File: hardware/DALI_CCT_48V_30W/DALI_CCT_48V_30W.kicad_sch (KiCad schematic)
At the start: 0 parts

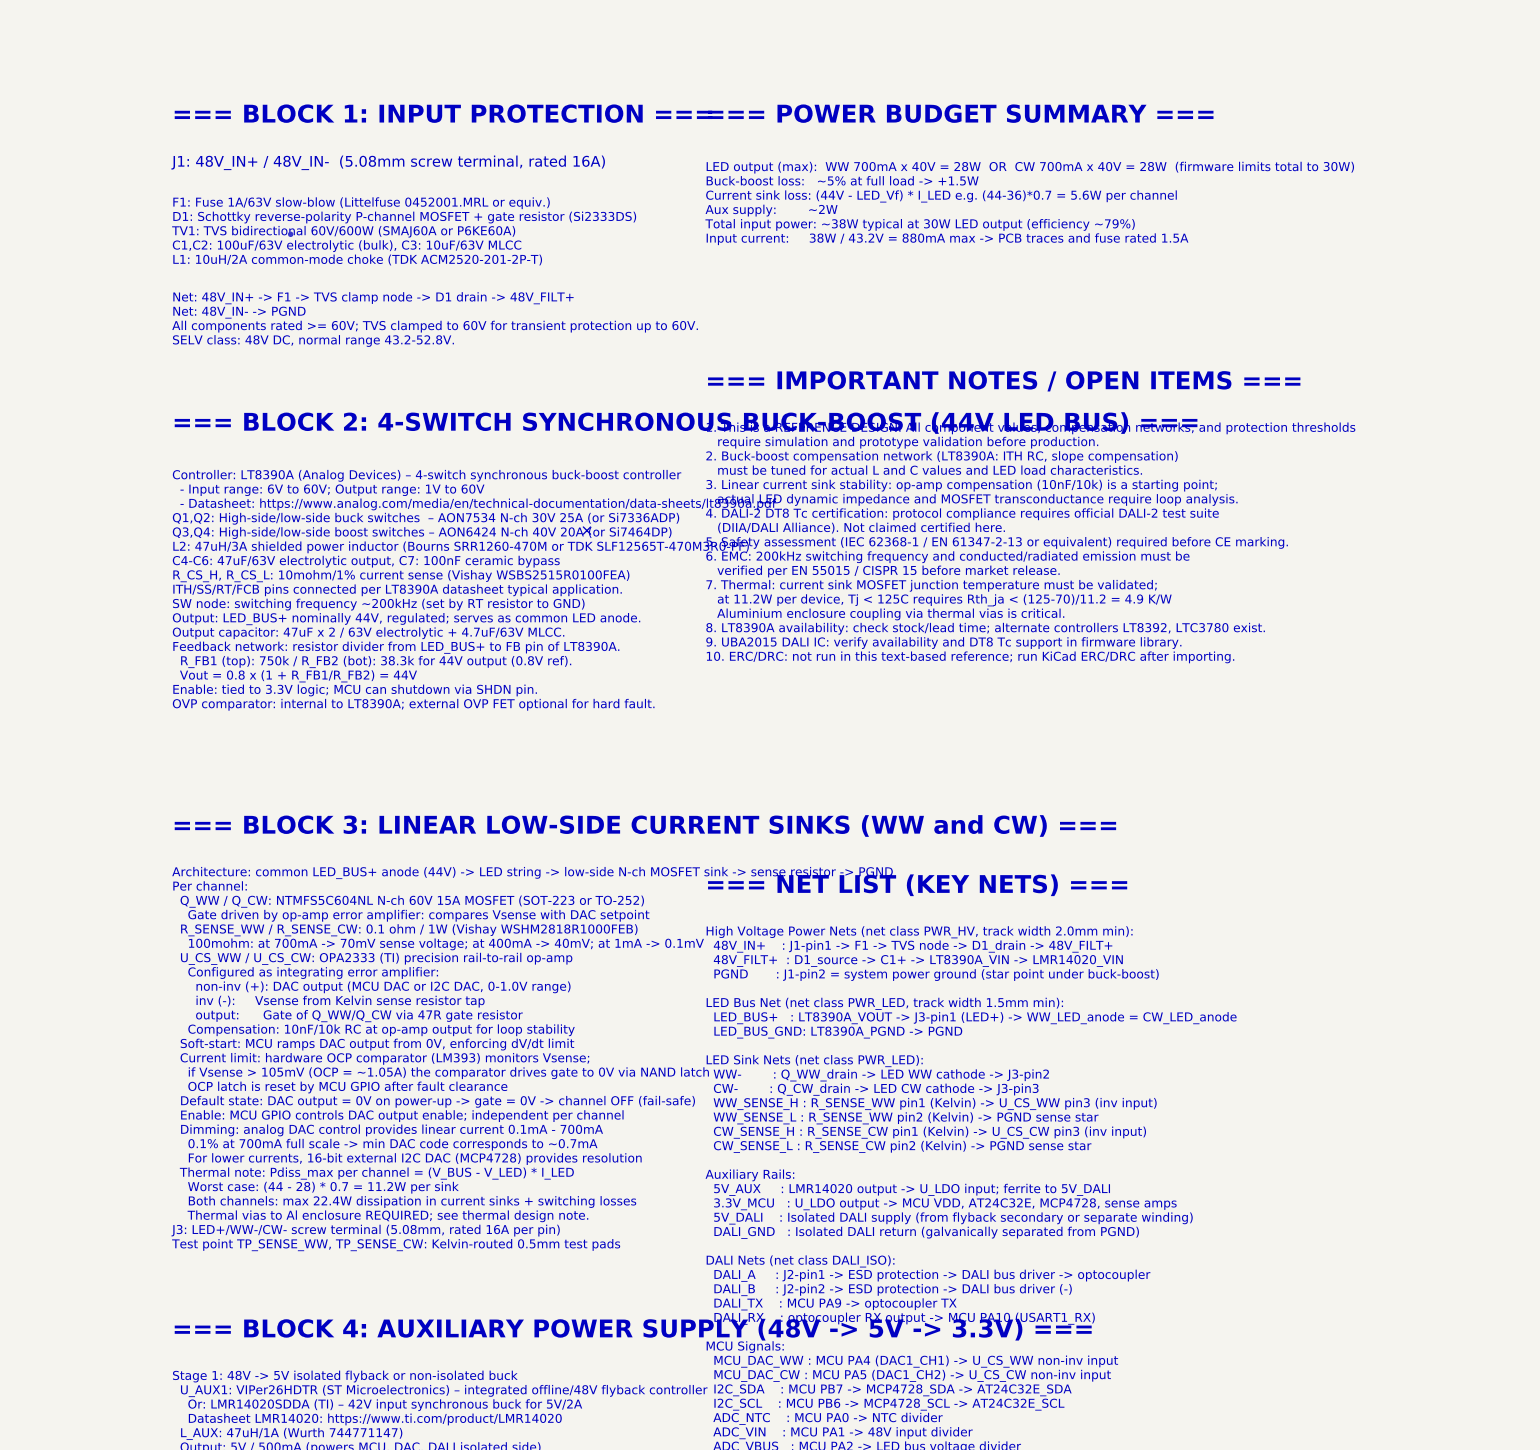
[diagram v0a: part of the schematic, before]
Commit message: Schritt 3: KiCad Schaltplan und PCB-Layout ergänzt (OI-011/OI-012)
Co-authored-by: manuelh83 <208121220+manuelh83@users.noreply.github.com>
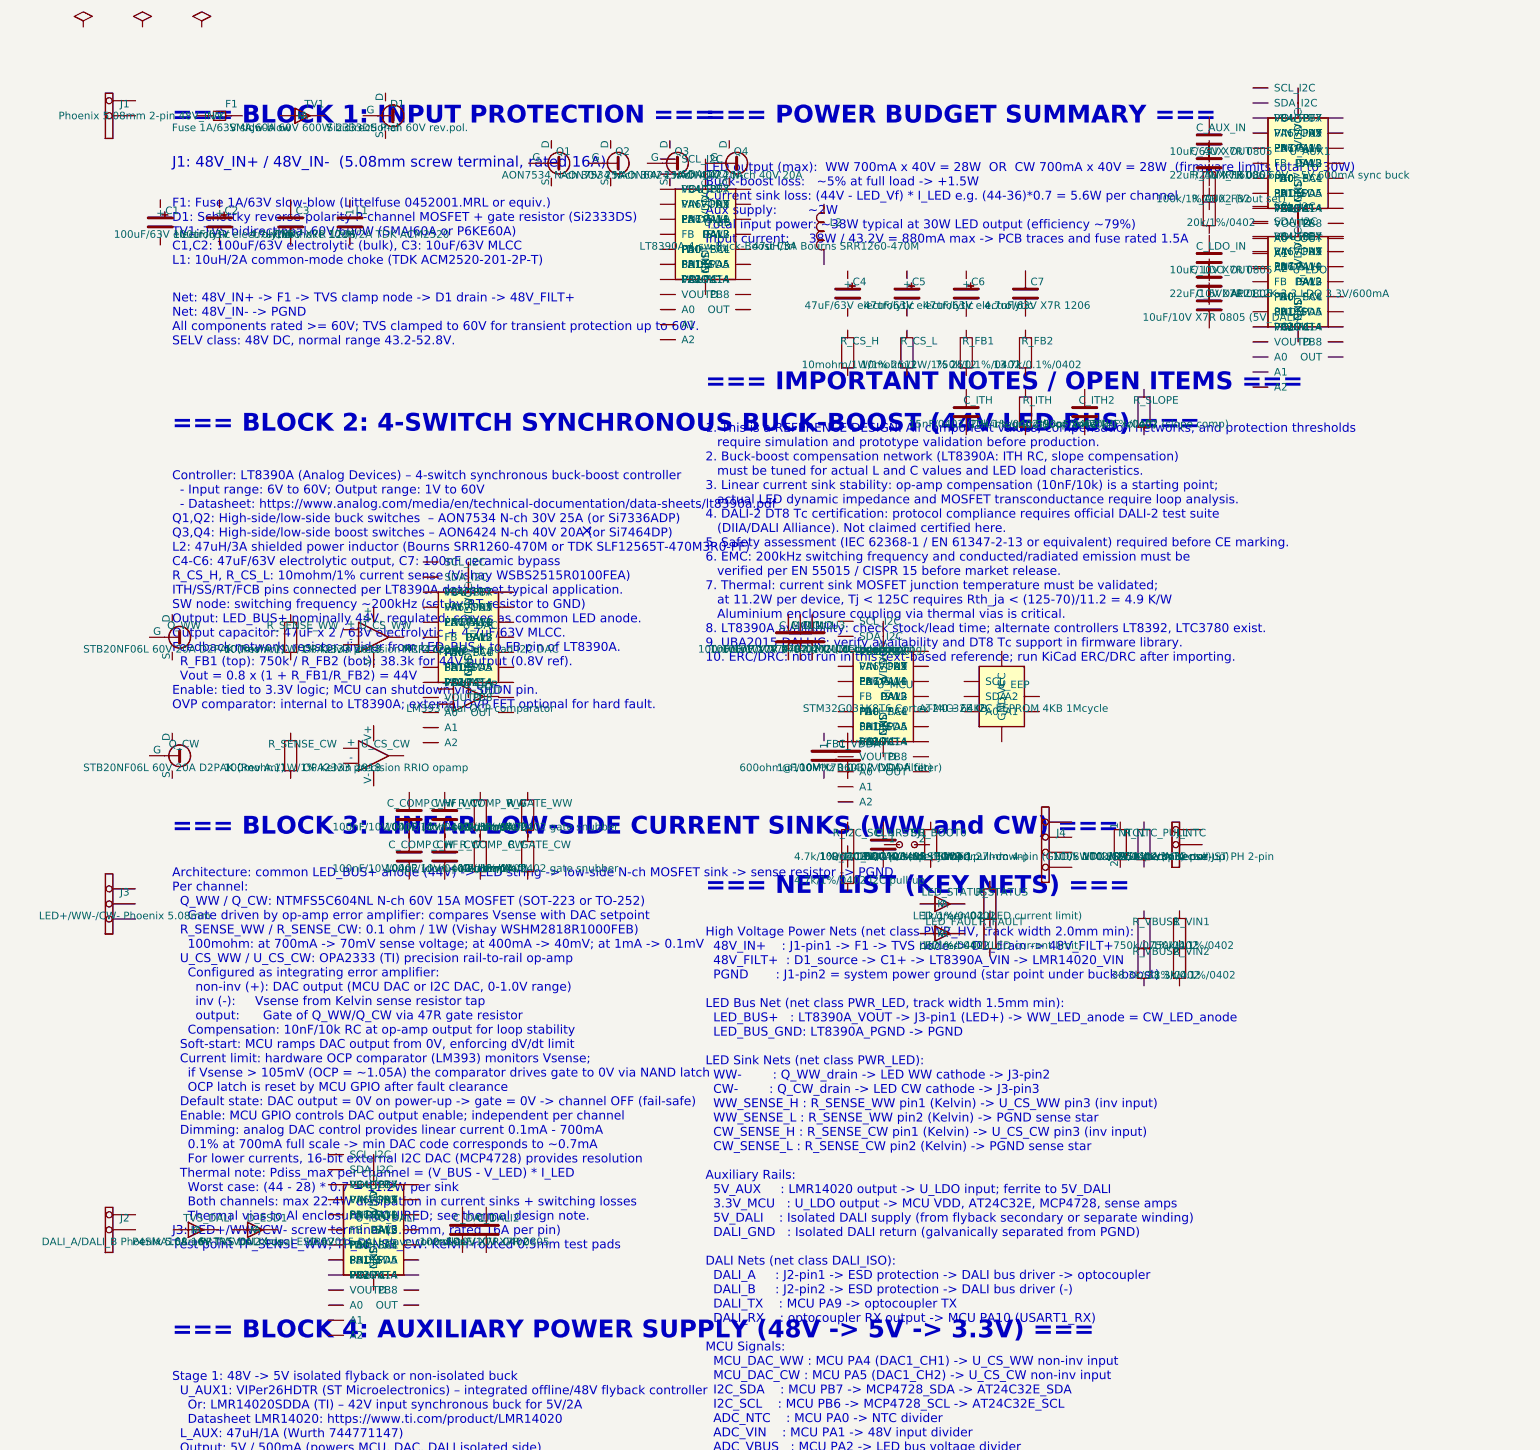
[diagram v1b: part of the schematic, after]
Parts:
- added C1, C2: 100uF/63V electrolytic, Capacitor_THT:CP_Radial_D5.0mm_P2.50mm, symbol Device:CP
- added C3, C7: 4.7uF/63V X7R 1206, Capacitor_SMD:C_1206_3216Metric, symbol Device:C
- added C4, C5, C6: 47uF/63V electrolytic, Capacitor_THT:CP_Radial_D5.0mm_P2.50mm, symbol Device:CP
- added C_5VDALI: 10uF/10V X7R 0805 (5V_DALI), Capacitor_SMD:C_0805_2012Metric, symbol Device:C
- added C_AUX_IN: 10uF/63V X7R 0805, Capacitor_SMD:C_0805_2012Metric, symbol Device:C
- added C_AUX_OUT: 22uF/25V X7R 0805, Capacitor_SMD:C_0805_2012Metric, symbol Device:C
- added C_COMP_CW, C_COMP_WW: 100nF/10V/0402 (dom.pole comp), Capacitor_SMD:C_0402_1005Metric, symbol Device:C
- added C_DALI1: 100nF/10V X7R 0402, Capacitor_SMD:C_0402_1005Metric, symbol Device:C
- added C_DALI2, C_LDO_IN: 10uF/10V X7R 0805, Capacitor_SMD:C_0805_2012Metric, symbol Device:C
- added C_HF_CW, C_HF_WW: 100pF/10V/0402 (HF rolloff), Capacitor_SMD:C_0402_1005Metric, symbol Device:C
- added C_ITH: 15nF/0402 (ITH integrator), Capacitor_SMD:C_0402_1005Metric, symbol Device:C
- added C_ITH2: 390pF/0402 (HF rolloff), Capacitor_SMD:C_0402_1005Metric, symbol Device:C
- added C_LDO_OUT: 22uF/10V X7R 0805, Capacitor_SMD:C_0805_2012Metric, symbol Device:C
- added C_MCU1, C_MCU2, C_MCU3: 100nF/10V X7R 0402 (MCU decoupling), Capacitor_SMD:C_0402_1005Metric, symbol Device:C
- added C_NRST: 100nF/10V/0402 (NRST filter), Capacitor_SMD:C_0402_1005Metric, symbol Device:C
- added C_VDDA: 1uF/10V X7R 0402 (VDDA filter), Capacitor_SMD:C_0402_1005Metric, symbol Device:C
- added D1: Si2333DS P-ch 60V rev.pol., Package_TO_SOT_SMD:SOT-23, symbol Device:MOSFET_P
- added D_ESD1: PRTR5V0U2X dual ESD 5V, Package_TO_SOT_SMD:SOT-363_Handsoldering, symbol Device:D_Schottky
- added F1: Fuse 1A/63V slow-blow, Fuse:Fuse_0402_1005Metric, symbol Device:Fuse
- added FB1: 600ohm@100MHz 0603 (VDDA filter), Inductor_SMD:L_0603_1608Metric, symbol Device:Ferrite_Bead
- added J1: Phoenix 5.08mm 2-pin 48V_IN, Connector_PinHeader_5.08mm:PinHeader_1x02_P5.08mm_Vertical, symbol Connector_Generic:Conn_01x02
- added J2: DALI_A/DALI_B Phoenix 5.08mm, Connector_PinHeader_5.08mm:PinHeader_1x02_P5.08mm_Vertical, symbol Connector_Generic:Conn_01x02
- added J3: LED+/WW-/CW- Phoenix 5.08mm, Connector_PinHeader_5.08mm:PinHeader_1x03_P5.08mm_Vertical, symbol Connector_Generic:Conn_01x03
- added J4: SWD 1.27mm 4-pin (GND/SWDIO/SWDCLK/3V3), Connector_PinHeader_1.27mm:PinHeader_1x04_P1.27mm_SMD, symbol Connector_Generic:Conn_01x04
- added J_NTC: NTC ext. connector JST PH 2-pin, Connector_JST:JST_PH_B2B-PH-K_1x02_P2.00mm_Vertical, symbol Connector_Generic:Conn_01x02
- added L1: CM choke 10uH/2A TDK ACM2520, Inductor_SMD:L_2520_6332Metric, symbol Device:Ferrite_Bead
- added L2: 47uH/3A Bourns SRR1260-470M, Inductor_SMD:L_Bourns_SRR1260, symbol Device:L
- added LED_FAULT: LED red 0402, LED_SMD:LED_0402_1005Metric, symbol Device:LED
- added LED_STATUS: LED green 0402, LED_SMD:LED_0402_1005Metric, symbol Device:LED
- added NTC1: 100k NTC B3950 (temp sense), Resistor_SMD:R_0402_1005Metric, symbol Device:R_Thermistor_NTC
- added Q1, Q2: AON7534 N-ch 30V 25A, Package_TO_SOT_SMD:DFN-8-1EP_3x3mm_P0.65mm, symbol Device:MOSFET_N
- added Q3, Q4: AON6424 N-ch 40V 20A, Package_TO_SOT_SMD:DFN-8-1EP_3x3mm_P0.65mm, symbol Device:MOSFET_N
- added Q_CW, Q_WW: STB20NF06L 60V 20A D2PAK (Rev A.1), Package_TO_SOT_SMD:TO-263-3_TabDown, symbol Device:MOSFET_N
- added R_AUX_FB1: 100k/1%/0402 (Vout set), Resistor_SMD:R_0402_1005Metric, symbol Device:R
- added R_AUX_FB2: 20k/1%/0402, Resistor_SMD:R_0402_1005Metric, symbol Device:R
- added R_BOOT0: 10k/1%/0402 (BOOT0 pull-down), Resistor_SMD:R_0402_1005Metric, symbol Device:R
- added R_COMP_CW, R_COMP_WW: 10k/1%/0402, Resistor_SMD:R_0402_1005Metric, symbol Device:R
- added R_CS_H, R_CS_L: 10mohm/1W/1% 2512, Resistor_SMD:R_2512_6332Metric, symbol Device:R
- added R_FAULT, R_STATUS: 1k/1%/0402 (LED current limit), Resistor_SMD:R_0402_1005Metric, symbol Device:R
- added R_FB1, R_VBUS1, R_VIN1: 750k/0.1%/0402, Resistor_SMD:R_0402_1005Metric, symbol Device:R
- added R_FB2: 13.7k/0.1%/0402, Resistor_SMD:R_0402_1005Metric, symbol Device:R
- added R_GATE_CW, R_GATE_WW: 47ohm/1%/0402 gate snubber, Resistor_SMD:R_0402_1005Metric, symbol Device:R
- added R_I2C_SCL, R_I2C_SDA: 4.7k/1%/0402 I2C pull-up, Resistor_SMD:R_0402_1005Metric, symbol Device:R
- added R_ITH: 22k/1%/0402 (loop xover), Resistor_SMD:R_0402_1005Metric, symbol Device:R
- added R_NTC_PULL: 100k/1%/0402 (NTC pull-up), Resistor_SMD:R_0402_1005Metric, symbol Device:R
- added R_SENSE_CW, R_SENSE_WW: 100mohm/1W/1% Kelvin 2818, Resistor_SMD:R_2818_7145Metric, symbol Device:R
- added R_SLOPE: 470k/1%/0402 (slope comp), Resistor_SMD:R_0402_1005Metric, symbol Device:R
- added R_VBUS2, R_VIN2: 38.3k/0.1%/0402, Resistor_SMD:R_0402_1005Metric, symbol Device:R
- added SJ1: BOOT0 solder jumper, Jumper:SolderJumper-2_P1.3mm_Open_RoundedPad1.0x1.5mm, symbol Device:Jumper_NO_Small
- added TV1: SMAJ60A 60V 600W bidirectional, Diode_SMD:D_SMA, symbol Device:D_TVS
- added TVS_DALI: P4SMA16A 16V TVS DALI bus, Diode_SMD:D_SMA, symbol Device:D_TVS
- added U_AUX1: LMR16006 60V->5V 600mA sync buck, Package_TO_SOT_SMD:SOT-23-5, symbol Device:IC
- added U_BB: LT8390A 4-sw Buck-Boost Ctrl, Package_SO:TSSOP-28_4.4x9.7mm_P0.65mm, symbol Device:IC
- added U_CS_CW, U_CS_WW: OPA2333 precision RRIO opamp, Package_SO:SOIC-8_3.9x4.9mm_P1.27mm, symbol Device:OPAMP
- added U_DAC: MCP4728 12-bit quad I2C DAC, Package_SO:MSOP-10_3x3mm_P0.5mm, symbol Device:IC
- added U_EEP: AT24C32E I2C EEPROM 4KB 1Mcycle, Package_SO:SOIC-8_3.9x4.9mm_P1.27mm, symbol Device:EEPROM_I2C
- added U_ISO_DALI: UBA2015 DALI slave controller, Package_SO:SO-8_3.9x4.9mm_P1.27mm, symbol Device:IC
- added U_LDO: AP2112K-3.3 LDO 3.3V/600mA, Package_TO_SOT_SMD:SOT-23-5, symbol Device:IC
- added U_MCU: STM32G031K8T6 Cortex-M0+ 64KB, Package_QFP:LQFP-32_7x7mm_P0.8mm, symbol Device:IC
- added U_OCP: LM393 dual OCP comparator, Package_SO:SOIC-8_3.9x4.9mm_P1.27mm, symbol Device:LM393
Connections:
- new net: U_DAC.DALI+, U_DAC.PA10, U_DAC.SW1
- new net: U_DAC.DALI-, U_DAC.PA13, U_DAC.SW2
- new net: U_DAC.EN, U_DAC.PA7, U_DAC.PB6
- new net: U_DAC.GND, U_DAC.NRST
- new net: U_DAC.ITH, U_DAC.PA0, U_DAC.PB0
- new net: U_DAC.PA1, U_DAC.PB1, U_DAC.SHDN
- new net: U_DAC.PA14, U_DAC.VOUTA
- new net: U_DAC.PA2, U_DAC.PB3, U_DAC.VOUTC
- new net: U_DAC.PA4, U_DAC.SCL
- new net: U_DAC.PA5, U_DAC.SDA
- new net: U_DAC.PA6, U_DAC.VIN
- new net: U_DAC.PA9, U_DAC.RX, U_DAC.VOUT
- new net: U_DAC.PB4, U_DAC.VOUTB
- new net: U_DAC.PB7, U_DAC.TX
- new net: U_BB.DALI+, U_BB.PA10, U_BB.SW1
- new net: U_BB.DALI-, U_BB.PA13, U_BB.SW2
- new net: U_BB.EN, U_BB.PA7, U_BB.PB6
- new net: U_BB.GND, U_BB.NRST
- new net: U_BB.ITH, U_BB.PA0, U_BB.PB0
- new net: U_BB.PA1, U_BB.PB1, U_BB.SHDN
- new net: U_BB.PA14, U_BB.VOUTA
- new net: U_BB.PA2, U_BB.PB3, U_BB.VOUTC
- new net: U_BB.PA4, U_BB.SCL
- new net: U_BB.PA5, U_BB.SDA
- new net: U_BB.PA6, U_BB.VIN
- new net: U_BB.PA9, U_BB.RX, U_BB.VOUT
- new net: U_BB.PB4, U_BB.VOUTB
- new net: U_BB.PB7, U_BB.TX
- new net: U_LDO.DALI+, U_LDO.PA10, U_LDO.SW1
- new net: U_LDO.DALI-, U_LDO.PA13, U_LDO.SW2
- new net: U_LDO.EN, U_LDO.PA7, U_LDO.PB6
- new net: U_LDO.GND, U_LDO.NRST
- new net: U_LDO.ITH, U_LDO.PA0, U_LDO.PB0
- new net: U_LDO.PA1, U_LDO.PB1, U_LDO.SHDN
- new net: U_LDO.PA14, U_LDO.VOUTA
- new net: U_LDO.PA2, U_LDO.PB3, U_LDO.VOUTC
- new net: U_LDO.PA4, U_LDO.SCL
- new net: U_LDO.PA5, U_LDO.SDA
- new net: U_LDO.PA6, U_LDO.VIN
- new net: U_LDO.PA9, U_LDO.RX, U_LDO.VOUT
- new net: U_LDO.PB4, U_LDO.VOUTB
- new net: U_LDO.PB7, U_LDO.TX
- new net: U_ISO_DALI.DALI+, U_ISO_DALI.PA10, U_ISO_DALI.SW1
- new net: U_ISO_DALI.DALI-, U_ISO_DALI.PA13, U_ISO_DALI.SW2
- new net: U_ISO_DALI.EN, U_ISO_DALI.PA7, U_ISO_DALI.PB6
- new net: U_ISO_DALI.GND, U_ISO_DALI.NRST
- new net: U_ISO_DALI.ITH, U_ISO_DALI.PA0, U_ISO_DALI.PB0
- new net: U_ISO_DALI.PA1, U_ISO_DALI.PB1, U_ISO_DALI.SHDN
- new net: U_ISO_DALI.PA14, U_ISO_DALI.VOUTA
- new net: U_ISO_DALI.PA2, U_ISO_DALI.PB3, U_ISO_DALI.VOUTC
- new net: U_ISO_DALI.PA4, U_ISO_DALI.SCL
- new net: U_ISO_DALI.PA5, U_ISO_DALI.SDA
- new net: U_ISO_DALI.PA6, U_ISO_DALI.VIN
- new net: U_ISO_DALI.PA9, U_ISO_DALI.RX, U_ISO_DALI.VOUT
- new net: U_ISO_DALI.PB4, U_ISO_DALI.VOUTB
- new net: U_ISO_DALI.PB7, U_ISO_DALI.TX
- new net: U_MCU.DALI+, U_MCU.PA10, U_MCU.SW1
- new net: U_MCU.DALI-, U_MCU.PA13, U_MCU.SW2
- new net: U_MCU.EN, U_MCU.PA7, U_MCU.PB6
- new net: U_MCU.GND, U_MCU.NRST
- new net: U_MCU.ITH, U_MCU.PA0, U_MCU.PB0
- new net: U_MCU.PA1, U_MCU.PB1, U_MCU.SHDN
- new net: U_MCU.PA14, U_MCU.VOUTA
- new net: U_MCU.PA2, U_MCU.PB3, U_MCU.VOUTC
- new net: U_MCU.PA4, U_MCU.SCL
- new net: U_MCU.PA5, U_MCU.SDA
- new net: U_MCU.PA6, U_MCU.VIN
- new net: U_MCU.PA9, U_MCU.RX, U_MCU.VOUT
- new net: U_MCU.PB4, U_MCU.VOUTB
- new net: U_MCU.PB7, U_MCU.TX
- new net: U_AUX1.DALI+, U_AUX1.PA10, U_AUX1.SW1
- new net: U_AUX1.DALI-, U_AUX1.PA13, U_AUX1.SW2
- new net: U_AUX1.EN, U_AUX1.PA7, U_AUX1.PB6
- new net: U_AUX1.GND, U_AUX1.NRST
- new net: U_AUX1.ITH, U_AUX1.PA0, U_AUX1.PB0
- new net: U_AUX1.PA1, U_AUX1.PB1, U_AUX1.SHDN
- new net: U_AUX1.PA14, U_AUX1.VOUTA
- new net: U_AUX1.PA2, U_AUX1.PB3, U_AUX1.VOUTC
- new net: U_AUX1.PA4, U_AUX1.SCL
- new net: U_AUX1.PA5, U_AUX1.SDA
- new net: U_AUX1.PA6, U_AUX1.VIN
- new net: U_AUX1.PA9, U_AUX1.RX, U_AUX1.VOUT
- new net: U_AUX1.PB4, U_AUX1.VOUTB
- new net: U_AUX1.PB7, U_AUX1.TX
